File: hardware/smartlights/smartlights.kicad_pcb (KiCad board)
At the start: 2 copper layers, 40 x 65 mm, 23 parts, among them J1 Conn_01x02_MountingPin, J10 Conn_Coaxial_Power, J11 Raspberry_Pi_2_3, J2 Conn_01x04, J3 Conn_01x02_MountingPin, J4 Conn_01x02_MountingPin, J5 Conn_01x02_MountingPin, J6 Conn_01x02_MountingPin, J7 Conn_01x02_MountingPin, J8 Conn_01x02_MountingPin, J9 Conn_01x02_MountingPin, Q1 IRLZ34N, Q2 IRLZ34N, Q3 IRLZ34N, Q4 IRLZ34N, Q5 IRLZ34N, Q6 IRLZ34N, SW1 SW_Push, U1 LM2596T-5

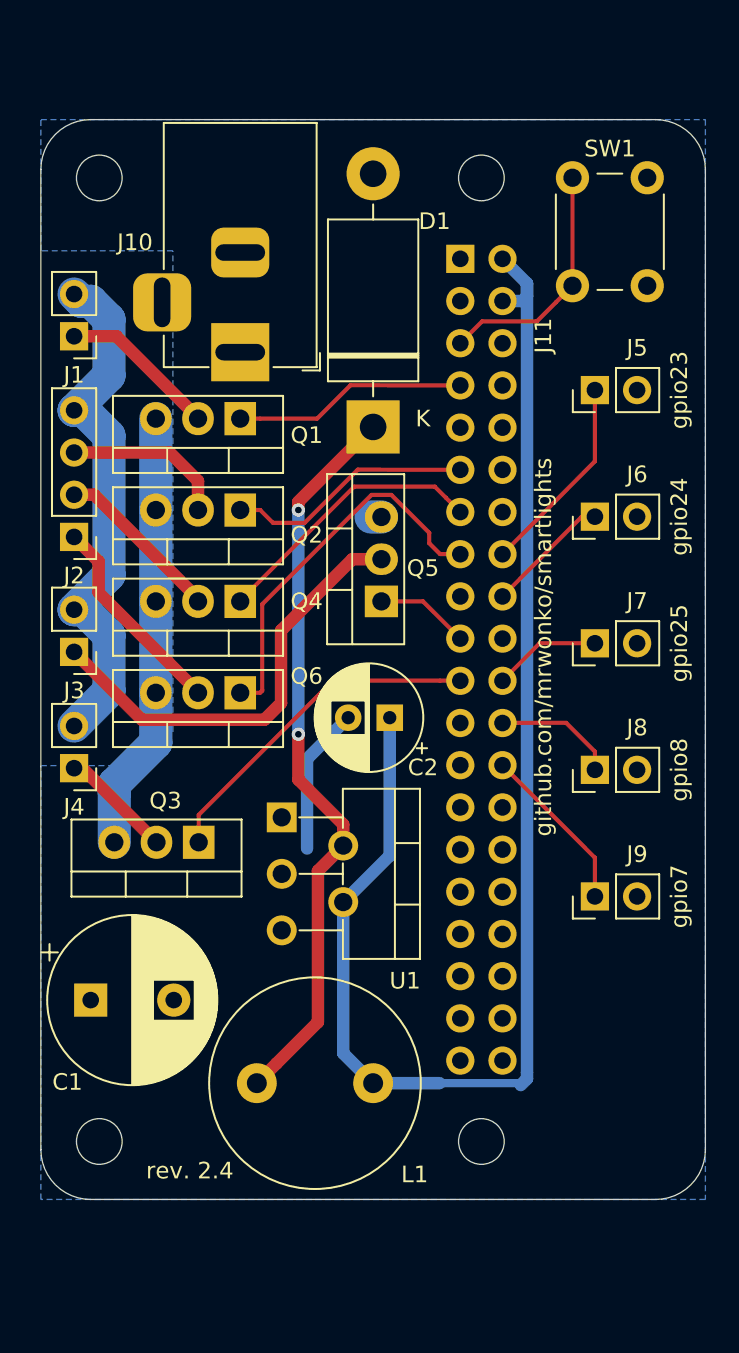
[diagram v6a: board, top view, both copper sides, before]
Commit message: SMD Rework
- removed one button to make space
- slightly larger PCB dimensions
- SMD transistor & voltage regulator
- access to individual RGB channels
- second RGB output
- two additional single-color outputs
- power jack moved closer towards edge
- custom footprints for light connectors
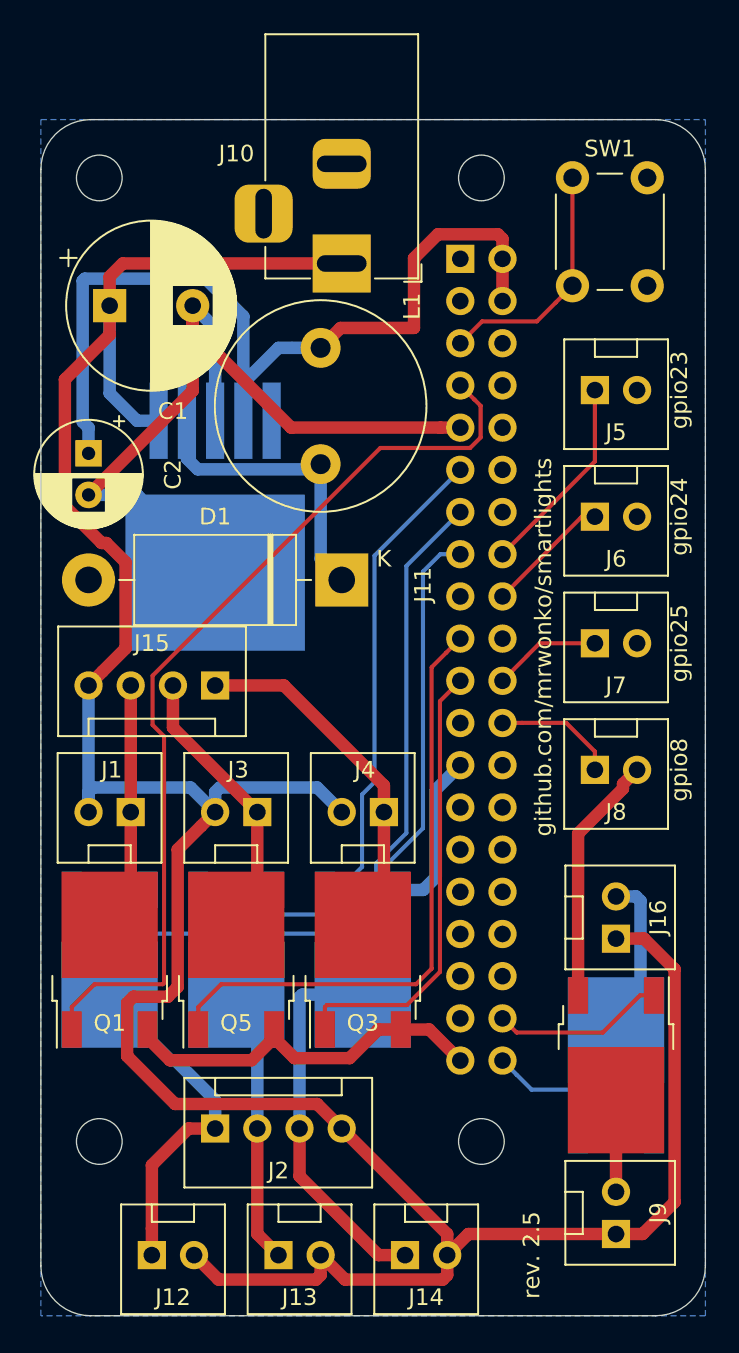
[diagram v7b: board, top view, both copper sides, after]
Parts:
- added J12: Conn_01x02_MountingPin, smartlights:PinHeader_1x02_P2.54mm_Vertical_Lock, F.Cu at (106.7, 133.3)
- added J13: Conn_01x02_MountingPin, smartlights:PinHeader_1x02_P2.54mm_Vertical_Lock, F.Cu at (114.3, 133.3)
- added J14: Conn_01x02_MountingPin, smartlights:PinHeader_1x02_P2.54mm_Vertical_Lock, F.Cu at (121.9, 133.3)
- added J15: Conn_01x04, smartlights:PinHeader_1x04_P2.54mm_Vertical_Lock, F.Cu at (110.5, 99.1)
- added J16: Conn_01x02_MountingPin, smartlights:PinHeader_1x02_P2.54mm_Vertical_Lock, F.Cu at (134.6, 114.3)
- added Q7: IRLZ34N, smartlights:TO-252AA, B.Cu at (134.6, 121.9)
- added Q8: IRLZ34N, smartlights:TO-252AA, F.Cu at (134.6, 121.9)
- J1, J3, J4, J5, J6, J7, J8, J9: footprint Connector_PinHeader_2.54mm:PinHeader_1x02_P2.54mm_Vertical -> smartlights:PinHeader_1x02_P2.54mm_Vertical_Lock
- J2: footprint Connector_PinHeader_2.54mm:PinHeader_1x04_P2.54mm_Vertical -> smartlights:PinHeader_1x04_P2.54mm_Vertical_Lock
- Q1, Q3, Q5: footprint Package_TO_SOT_THT:TO-220-3_Vertical -> smartlights:TO-252AA
- Q2, Q4, Q6: footprint Package_TO_SOT_THT:TO-220-3_Vertical -> smartlights:TO-252AA; moved to B.Cu
- U1: footprint Package_TO_SOT_THT:TO-220-5_P3.4x3.7mm_StaggerOdd_Lead3.8mm_Vertical -> Package_TO_SOT_SMD:TO-263-5_TabPin3; moved to B.Cu
- moved L1 44.4 mm to (116.8, 78.7), turned to 270 degrees
- moved C1 41.8 mm to (104.1, 76.2)
- moved J2 36.6 mm to (110.5, 125.7), turned to 90 degrees
- moved Q1 33.5 mm to (104.1, 115.6), turned to 90 degrees
- moved J1 28.8 mm to (105.4, 106.7), turned to 270 degrees
- moved Q2 28.1 mm to (119.4, 115.6), turned to 270 degrees
- moved C2 24.1 mm to (102.9, 85.1), turned to 270 degrees
- moved Q5 23.3 mm to (111.8, 115.6)
- moved Q4 21.6 mm to (111.8, 115.6), turned to 270 degrees
- moved J9 20.4 mm to (134.6, 132.1), turned to 180 degrees
- moved J4 18.8 mm to (120.7, 106.7), turned to 270 degrees
- moved U1 18.5 mm to (110.5, 88.9)
- moved Q6 17.9 mm to (104.1, 115.6), turned to 270 degrees
- moved J3 14.6 mm to (113.0, 106.7), turned to 270 degrees
- moved Q3 12.1 mm to (119.4, 115.6), turned to 90 degrees
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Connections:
- net /GND_B renamed /GND_B1
- net /GND_G renamed /GND_G1
- net /GND_R renamed /GND_R1
- net /PWR_19 renamed /GND_G2
- net /PWR_21 renamed /GND_R2
- net /PWR_7 renamed /GND_B2
- J11 pad 26: pin26 -> Net-(J11-Pad26)
- J11 pad 38: Net-(J11-Pad38) -> pin38
- J11 pad 40: Net-(J11-Pad40) -> pin40
- J9 pad 1: pin26 -> 12V
- J9 pad 2: GND -> /GND_38
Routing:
- net 12V: track 32.2 -> 173.7 mm
- net GND: track 37.8 -> 98.8 mm
- net pin7: track 14.1 -> 55.6 mm
- net pin19: track 5.67 -> 36.9 mm
- net 5V: track 85.7 -> 55.4 mm
- net /5V_raw: track 44.6 -> 18.2 mm, vias 2 -> 0
- net pin15: track 23.1 -> 44.6 mm
- net pin13: track 16.8 -> 36.4 mm
- net /GND_R2: track 6.81 -> 21.6 mm
- net pin11: track 14.9 -> 29.2 mm
- net /GND_B1: track 9.92 -> 23.0 mm
- net pin40: track 0.00 -> 11.0 mm
- net pin38: track 0.00 -> 10.4 mm
- net pin26: track 10.2 -> 0.00 mm
- net /GND_40: track 0.00 -> 9.99 mm
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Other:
- board size 40 x 65 mm -> 40 x 72 mm
- board text added: "rev. 2.5"
- board text removed: "gpio7"
- board text removed: "rev. 2.4"
